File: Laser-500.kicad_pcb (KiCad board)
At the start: 2 copper layers, 17 parts, among them U1 Z80CPU, U10 TMM4164AP-15, U11 TMM4164AP-15, U12 TMM4164AP-15, U13 TMM4164AP-15, U14 TMM4164AP-15, U15 TMM4164AP-15, U16 TMM4164AP-15, U17 TMM4164AP-15, U2 74LS244, U3 74LS257, U4 74LS00, U5 27128, U6 74LS257, U7 27128, U8 74LS273, U9 2764

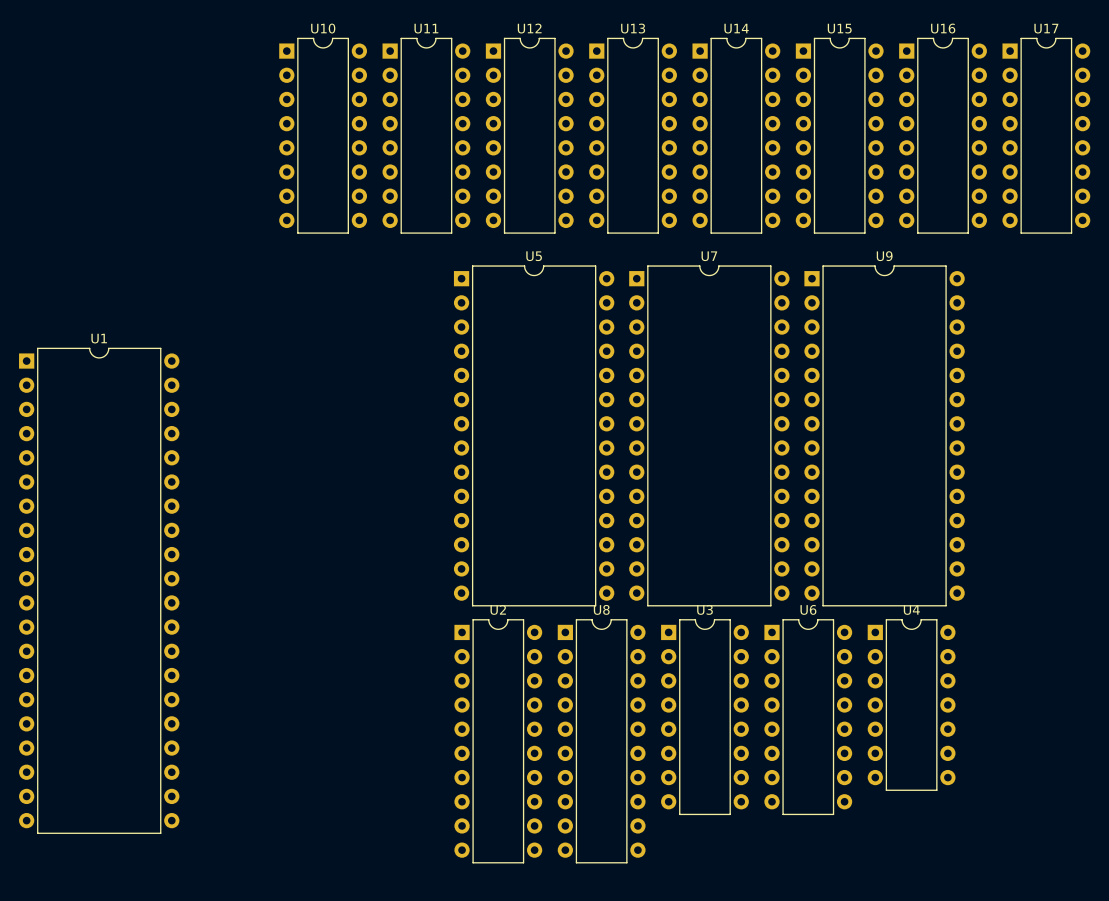
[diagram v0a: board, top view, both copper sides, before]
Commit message: Started video_cassette sch
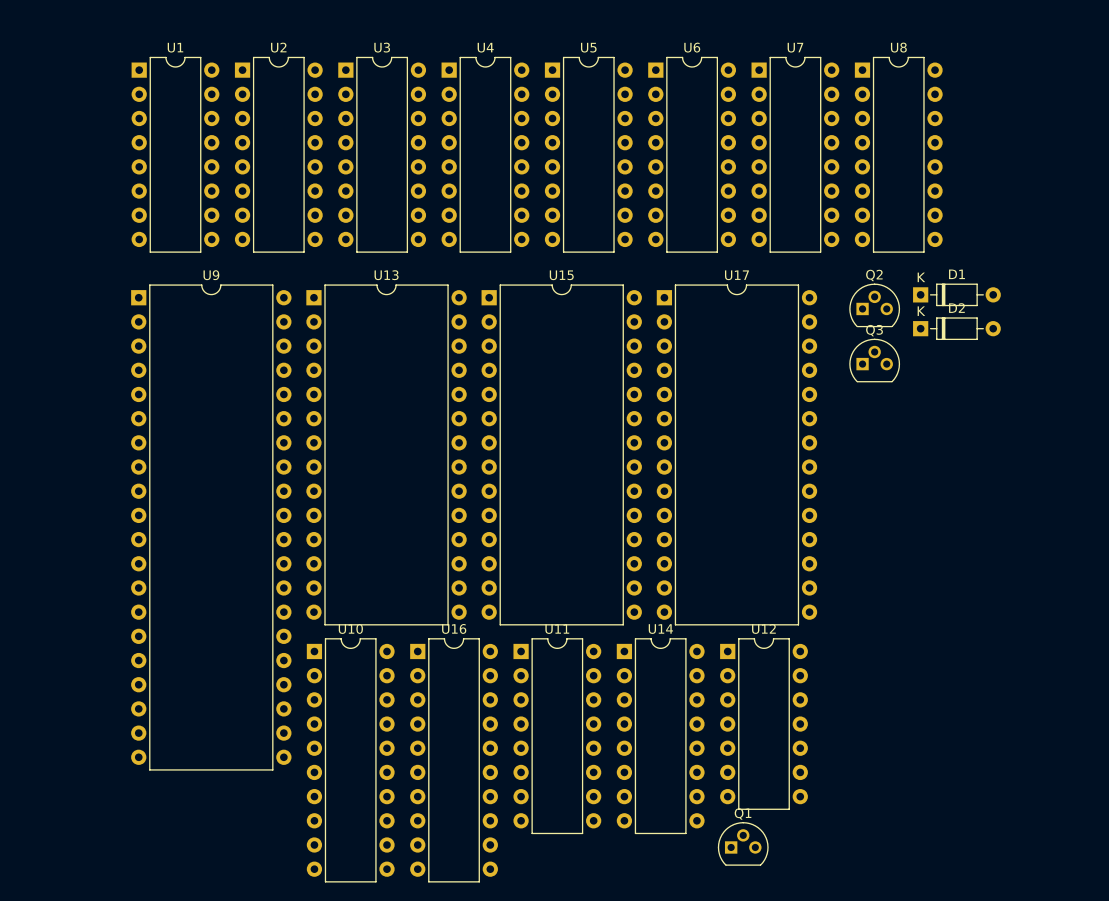
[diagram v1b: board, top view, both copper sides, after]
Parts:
- added D1: 1N4150, Diode_THT:D_DO-35_SOD27_P7.62mm_Horizontal, F.Cu at (164.1, 72.3)
- added D2: 1N4150, Diode_THT:D_DO-35_SOD27_P7.62mm_Horizontal, F.Cu at (164.1, 75.9)
- added Q1: 9018G, Package_TO_SOT_THT:TO-92, F.Cu at (144.2, 130.3)
- added Q2: 1402D, Package_TO_SOT_THT:TO-92, F.Cu at (158.0, 73.8)
- added Q3: 1402D, Package_TO_SOT_THT:TO-92, F.Cu at (158.0, 79.6)
- U1: value Z80CPU -> TMM4164AP-15; footprint Package_DIP:DIP-40_W15.24mm -> Package_DIP:DIP-16_W7.62mm
- U10: value TMM4164AP-15 -> 74LS244; footprint Package_DIP:DIP-16_W7.62mm -> Package_DIP:DIP-20_W7.62mm
- U11, U14: value TMM4164AP-15 -> 74LS257
- U12: value TMM4164AP-15 -> 74LS00; footprint Package_DIP:DIP-16_W7.62mm -> Package_DIP:DIP-14_W7.62mm
- U13, U15: value TMM4164AP-15 -> 27128; footprint Package_DIP:DIP-16_W7.62mm -> Package_DIP:DIP-28_W15.24mm
- U16: value TMM4164AP-15 -> 74LS273; footprint Package_DIP:DIP-16_W7.62mm -> Package_DIP:DIP-20_W7.62mm
- U17: value TMM4164AP-15 -> 2764; footprint Package_DIP:DIP-16_W7.62mm -> Package_DIP:DIP-28_W15.24mm
- U2: value 74LS244 -> TMM4164AP-15; footprint Package_DIP:DIP-20_W7.62mm -> Package_DIP:DIP-16_W7.62mm
- U3, U6: value 74LS257 -> TMM4164AP-15
- U4: value 74LS00 -> TMM4164AP-15; footprint Package_DIP:DIP-14_W7.62mm -> Package_DIP:DIP-16_W7.62mm
- U5, U7: value 27128 -> TMM4164AP-15; footprint Package_DIP:DIP-28_W15.24mm -> Package_DIP:DIP-16_W7.62mm
- U8: value 74LS273 -> TMM4164AP-15; footprint Package_DIP:DIP-20_W7.62mm -> Package_DIP:DIP-16_W7.62mm
- U9: value 2764 -> Z80CPU; footprint Package_DIP:DIP-28_W15.24mm -> Package_DIP:DIP-40_W15.24mm
- moved U16 81.3 mm to (111.3, 109.8)
- moved U4 74.1 mm to (114.6, 48.7)
- moved U9 70.7 mm to (82.0, 72.6)
- moved U3 68.1 mm to (103.8, 48.7)
- moved U12 67.7 mm to (143.9, 109.8)
- moved U8 66.8 mm to (158.0, 48.7)
- moved U11 64.5 mm to (122.2, 109.8)
- moved U14 63.5 mm to (133.0, 109.8)
- moved U2 63.4 mm to (92.9, 48.7)
- moved U10 63.1 mm to (100.5, 109.8)
- moved U6 60.3 mm to (136.3, 48.7)
- moved U17 44.6 mm to (137.2, 72.6)
- moved U15 42.0 mm to (118.8, 72.6)
- moved U13 39.4 mm to (100.4, 72.6)
- moved U1 32.8 mm to (82.1, 48.7)
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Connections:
- U1 pad 10: unconnected-(U1-D6-Pad10) -> MA5
- U1 pad 11: unconnected-(U1-VCC-Pad11) -> MA4
- U1 pad 12: unconnected-(U1-D2-Pad12) -> MA3
- U1 pad 13: unconnected-(U1-D7-Pad13) -> MA6
- U1 pad 14: unconnected-(U1-D0-Pad14) -> RD0
- U1 pad 15: unconnected-(U1-D1-Pad15) -> ~{CAS}
- U1 pad 16: unconnected-(U1-~{INT}-Pad16) -> <NO NET>
- U1 pad 2: unconnected-(U1-A12-Pad2) -> RD0
- U1 pad 3: unconnected-(U1-A13-Pad3) -> ~{RAMW}
- U1 pad 4: unconnected-(U1-A14-Pad4) -> ~{RAS}
- U1 pad 5: unconnected-(U1-A15-Pad5) -> MA0
- U1 pad 6: unconnected-(U1-~{CLK}-Pad6) -> MA2
- U1 pad 7: unconnected-(U1-D4-Pad7) -> MA1
- U1 pad 8: unconnected-(U1-D3-Pad8) -> +5V
- U1 pad 9: unconnected-(U1-D5-Pad9) -> MA7
- U10 pad 14: RD0 -> unconnected-(U10-O2a-Pad14)
- U10 pad 16: <NO NET> -> unconnected-(U10-O1a-Pad16)
- U10 pad 2: RD0 -> unconnected-(U10-I0a-Pad2)
- U10 pad 8: <NO NET> -> unconnected-(U10-I3a-Pad8)
- U11 pad 14: RD1 -> unconnected-(U11-I0c-Pad14)
- U11 pad 16: <NO NET> -> unconnected-(U11-VCC-Pad16)
- U11 pad 2: RD1 -> unconnected-(U11-I0a-Pad2)
- U11 pad 8: <NO NET> -> unconnected-(U11-GND-Pad8)
- U12 pad 14: RD1 -> (no net)
- U12 pad 2: RD1 -> unconnected-(U12-Pad2)
- U12 pad 7: unconnected-(U12-A1-Pad7) -> (no net)
- U12 pad 8: <NO NET> -> unconnected-(U12-Pad8)
- U13 pad 14: RD2 -> unconnected-(U13-GND-Pad14)
- U13 pad 16: <NO NET> -> unconnected-(U13-D4-Pad16)
- U13 pad 2: RD2 -> unconnected-(U13-A12-Pad2)
- U13 pad 8: <NO NET> -> unconnected-(U13-A2-Pad8)
- U14 pad 16: <NO NET> -> unconnected-(U14-VCC-Pad16)
- U14 pad 8: <NO NET> -> unconnected-(U14-GND-Pad8)
- U15 pad 16: <NO NET> -> unconnected-(U15-D4-Pad16)
- U15 pad 8: <NO NET> -> unconnected-(U15-A2-Pad8)
- U16 pad 16: <NO NET> -> unconnected-(U16-Q6-Pad16)
- U16 pad 8: <NO NET> -> unconnected-(U16-D3-Pad8)
- U17 pad 16: <NO NET> -> unconnected-(U17-D4-Pad16)
- U17 pad 8: <NO NET> -> unconnected-(U17-A2-Pad8)
- U2 pad 10: unconnected-(U2-GND-Pad10) -> MA5
- U2 pad 11: unconnected-(U2-I0b-Pad11) -> MA4
- U2 pad 12: unconnected-(U2-O3a-Pad12) -> MA3
- U2 pad 13: unconnected-(U2-I1b-Pad13) -> MA6
- U2 pad 14: unconnected-(U2-O2a-Pad14) -> RD1
- U2 pad 15: unconnected-(U2-I2b-Pad15) -> ~{CAS}
- U2 pad 16: unconnected-(U2-O1a-Pad16) -> <NO NET>
- U2 pad 2: unconnected-(U2-I0a-Pad2) -> RD1
- U2 pad 3: unconnected-(U2-O3b-Pad3) -> ~{RAMW}
- U2 pad 4: unconnected-(U2-I1a-Pad4) -> ~{RAS}
- U2 pad 5: unconnected-(U2-O2b-Pad5) -> MA0
- U2 pad 6: unconnected-(U2-I2a-Pad6) -> MA2
- U2 pad 7: unconnected-(U2-O1b-Pad7) -> MA1
- U2 pad 8: unconnected-(U2-I3a-Pad8) -> +5V
- U2 pad 9: unconnected-(U2-O0b-Pad9) -> MA7
- U3 pad 10: unconnected-(U3-I1d-Pad10) -> MA5
- U3 pad 11: unconnected-(U3-I0d-Pad11) -> MA4
- U3 pad 12: unconnected-(U3-Zc-Pad12) -> MA3
- U3 pad 13: unconnected-(U3-I1c-Pad13) -> MA6
- U3 pad 14: unconnected-(U3-I0c-Pad14) -> RD2
- U3 pad 15: unconnected-(U3-OE-Pad15) -> ~{CAS}
- U3 pad 16: unconnected-(U3-VCC-Pad16) -> <NO NET>
- U3 pad 2: unconnected-(U3-I0a-Pad2) -> RD2
- U3 pad 3: unconnected-(U3-I1a-Pad3) -> ~{RAMW}
- U3 pad 4: unconnected-(U3-Za-Pad4) -> ~{RAS}
- U3 pad 5: unconnected-(U3-I0b-Pad5) -> MA0
- U3 pad 6: unconnected-(U3-I1b-Pad6) -> MA2
- U3 pad 7: unconnected-(U3-Zb-Pad7) -> MA1
- U3 pad 8: unconnected-(U3-GND-Pad8) -> +5V
- U3 pad 9: unconnected-(U3-Zd-Pad9) -> MA7
- U4 pad 10: unconnected-(U4-Pad10) -> MA5
- U4 pad 11: unconnected-(U4-Pad11) -> MA4
- U4 pad 12: unconnected-(U4-Pad12) -> MA3
- U4 pad 13: unconnected-(U4-Pad13) -> MA6
- U4 pad 14: (no net) -> RD3
- U4 pad 2: unconnected-(U4-Pad2) -> RD3
- U4 pad 3: unconnected-(U4-Pad3) -> ~{RAMW}
- U4 pad 4: unconnected-(U4-Pad4) -> ~{RAS}
- U4 pad 5: unconnected-(U4-Pad5) -> MA0
- U4 pad 6: unconnected-(U4-Pad6) -> MA2
- U4 pad 7: (no net) -> MA1
- U4 pad 8: unconnected-(U4-Pad8) -> +5V
- U4 pad 9: unconnected-(U4-Pad9) -> MA7
- U5 pad 10: unconnected-(U5-A0-Pad10) -> MA5
- U5 pad 11: unconnected-(U5-D0-Pad11) -> MA4
- U5 pad 12: unconnected-(U5-D1-Pad12) -> MA3
- U5 pad 13: unconnected-(U5-D2-Pad13) -> MA6
- U5 pad 14: unconnected-(U5-GND-Pad14) -> RD4
- U5 pad 15: unconnected-(U5-D3-Pad15) -> ~{CAS}
- U5 pad 16: unconnected-(U5-D4-Pad16) -> <NO NET>
- U5 pad 2: unconnected-(U5-A12-Pad2) -> RD4
- U5 pad 3: unconnected-(U5-A7-Pad3) -> ~{RAMW}
- U5 pad 4: unconnected-(U5-A6-Pad4) -> ~{RAS}
- U5 pad 5: unconnected-(U5-A5-Pad5) -> MA0
- U5 pad 6: unconnected-(U5-A4-Pad6) -> MA2
- U5 pad 7: unconnected-(U5-A3-Pad7) -> MA1
- U5 pad 8: unconnected-(U5-A2-Pad8) -> +5V
- U5 pad 9: unconnected-(U5-A1-Pad9) -> MA7
- U6 pad 10: unconnected-(U6-I1d-Pad10) -> MA5
- U6 pad 11: unconnected-(U6-I0d-Pad11) -> MA4
- U6 pad 12: unconnected-(U6-Zc-Pad12) -> MA3
- U6 pad 13: unconnected-(U6-I1c-Pad13) -> MA6
- U6 pad 14: unconnected-(U6-I0c-Pad14) -> RD5
- U6 pad 15: unconnected-(U6-OE-Pad15) -> ~{CAS}
- U6 pad 16: unconnected-(U6-VCC-Pad16) -> <NO NET>
- U6 pad 2: unconnected-(U6-I0a-Pad2) -> RD5
- U6 pad 3: unconnected-(U6-I1a-Pad3) -> ~{RAMW}
- U6 pad 4: unconnected-(U6-Za-Pad4) -> ~{RAS}
- U6 pad 5: unconnected-(U6-I0b-Pad5) -> MA0
- U6 pad 6: unconnected-(U6-I1b-Pad6) -> MA2
- U6 pad 7: unconnected-(U6-Zb-Pad7) -> MA1
- U6 pad 8: unconnected-(U6-GND-Pad8) -> +5V
- U6 pad 9: unconnected-(U6-Zd-Pad9) -> MA7
- U7 pad 10: unconnected-(U7-A0-Pad10) -> MA5
- U7 pad 11: unconnected-(U7-D0-Pad11) -> MA4
- U7 pad 12: unconnected-(U7-D1-Pad12) -> MA3
- U7 pad 13: unconnected-(U7-D2-Pad13) -> MA6
- U7 pad 14: unconnected-(U7-GND-Pad14) -> RD6
- U7 pad 15: unconnected-(U7-D3-Pad15) -> ~{CAS}
- U7 pad 16: unconnected-(U7-D4-Pad16) -> <NO NET>
- U7 pad 2: unconnected-(U7-A12-Pad2) -> RD6
- U7 pad 3: unconnected-(U7-A7-Pad3) -> ~{RAMW}
- U7 pad 4: unconnected-(U7-A6-Pad4) -> ~{RAS}
- U7 pad 5: unconnected-(U7-A5-Pad5) -> MA0
- U7 pad 6: unconnected-(U7-A4-Pad6) -> MA2
- U7 pad 7: unconnected-(U7-A3-Pad7) -> MA1
- U7 pad 8: unconnected-(U7-A2-Pad8) -> +5V
- U7 pad 9: unconnected-(U7-A1-Pad9) -> MA7
- U8 pad 10: unconnected-(U8-GND-Pad10) -> MA5
- U8 pad 11: unconnected-(U8-Cp-Pad11) -> MA4
- U8 pad 12: unconnected-(U8-Q4-Pad12) -> MA3
- U8 pad 13: unconnected-(U8-D4-Pad13) -> MA6
- U8 pad 14: unconnected-(U8-D5-Pad14) -> RD7
- U8 pad 15: unconnected-(U8-Q5-Pad15) -> ~{CAS}
- U8 pad 16: unconnected-(U8-Q6-Pad16) -> <NO NET>
- U8 pad 2: unconnected-(U8-Q0-Pad2) -> RD7
- U8 pad 3: unconnected-(U8-D0-Pad3) -> ~{RAMW}
- U8 pad 4: unconnected-(U8-D1-Pad4) -> ~{RAS}
- U8 pad 5: unconnected-(U8-Q1-Pad5) -> MA0
- U8 pad 6: unconnected-(U8-Q2-Pad6) -> MA2
- U8 pad 7: unconnected-(U8-D2-Pad7) -> MA1
- U8 pad 8: unconnected-(U8-D3-Pad8) -> +5V
- U8 pad 9: unconnected-(U8-Q3-Pad9) -> MA7
